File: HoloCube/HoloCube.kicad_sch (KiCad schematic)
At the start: 26 parts, among them J1 ESPProgUART_RX, J2 Conn_01x08_MountingPin, J3 USB_C_Receptacle_USB2.0, U1 ESP32-PICO-D4, U2 LIS2DE12, U3 BH1750FVI-TR, U4 XC6209

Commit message: Place Parts
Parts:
- removed C?: (no value), symbol Device:C
- removed D2, D4: LED, LED_SMD:LED_0603_1608Metric, symbol Device:LED
- removed R?: (no value), symbol Device:R
- removed U2: LIS2DE12, Package_LGA:LGA-12_2x2mm_P0.5mm, symbol Sensor_Motion:LIS2DE12
- removed U3: BH1750FVI-TR, symbol KisonNew:BH1750FVI-TR
- added C4: (no value), symbol Device:C
- added C7, C8: (no value), Capacitor_SMD:C_0603_1608Metric, symbol Device:C
- added C9: TBD, Capacitor_SMD:C_0603_1608Metric, symbol Device:C
- added J4: (no value), symbol Connector:Micro_SD_Card
- added J5: (no value), symbol KisonNew:ESPProgJTAG_RX
- added JP1, JP2: (no value), symbol Jumper:Jumper_2_Bridged
- added R10, R11, R12, R13, R3, R9: (no value), symbol Device:R
- added R14, R15, R16, R17: 10k, Resistor_SMD:R_0603_1608Metric, symbol Device:R
- added U2: (no value), symbol LIS2DH12TR:LIS2DH12TR
- added U3: (no value), symbol BH1750FVI-TR:BH1750FVI-TR
- AE1: value Antenna -> (none); footprint RF_Antenna:Texas_SWRA117D_2.4GHz_Right -> (none)
- C1: value 10uf -> (none)
- C2: value 0.1uf -> (none)
- C3: value 0.1uF -> (none); footprint Capacitor_SMD:C_0603_1608Metric -> (none)
- C5, C6: value 1uf -> (none); footprint Capacitor_SMD:C_0603_1608Metric -> (none)
- D1: value WS2812B -> (none); footprint LED_SMD:LED_WS2812B_PLCC4_5.0x5.0mm_P3.2mm -> (none)
- D3: value D -> (none); footprint KisonNew:C8678 -> (none)
- J1: value ESPProgUART_RX -> (none); footprint KisonNew:IDC_1.27mm_6P -> (none)
- J2: value Conn_01x08_MountingPin -> (none)
- J3: value USB_C_Receptacle_USB2.0 -> (none); footprint Connector_USB:USB_C_Receptacle_HRO_TYPE-C-31-M-12 -> (none)
- R1: value 10k -> (none); footprint Resistor_SMD:R_0603_1608Metric -> (none)
- R2: value 0 -> (none)
- R4: value 0 -> (none); footprint Resistor_SMD:R_0603_1608Metric -> (none)
- R5, R8: value 10k -> (none); footprint Resistor_SMD:R_0603_1608Metric -> (none); LCSC (none) -> C429617
- R6, R7: value 5.1k -> (none); footprint Resistor_SMD:R_0603_1608Metric -> (none)
- U1: value ESP32-PICO-D4 -> (none); footprint Package_DFN_QFN:QFN-48-1EP_7x7mm_P0.5mm_EP5.3x5.3mm -> (none)
- U4: value XC6209 -> (none); footprint Package_TO_SOT_SMD:SOT-23-5 -> (none)
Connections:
- net +3.3VA: now also C1.1, C2.1, R3.2; no longer C1.2, C2.2
- net +3V3: now also J2.7 (Pin_7), R5.1, C4.1, J4.4 (VDD), J5.1 (VDD), JP2.1 (A), R12.2, R14.1, R15.1, R16.1, R17.1, R3.1, R9.1, U2.10 (VDD_IO), U2.2 (CS), U2.9 (VDD), U3.1 (VCC); no longer C1.1, C2.1
- net +5V: now also C5.1, J2.8 (Pin_8), U4.1 (VIN), U4.3 (CE)
- net DC: now also J2.5 (Pin_5), U1.22 (IO2), R10.1
- net GND: now also C1.2, C2.2, J2.6 (Pin_6), C4.2, C7.1, C9.1, J4.6 (VSS), J5.3 (GND), J5.5 (GND), J5.7 (GND), J5.9 (GND), JP1.1 (A), R10.2, R11.2, R13.2, U2.5 (RES), U2.6 (GND), U2.7 (GND), U2.8 (GND), U3.3 (GND)
- net I2C_SCL: now also R5.2, U1.13 (IO33), U2.1 (SCL/SPC), U3.6 (SCL)
- net I2C_SDA: now also R8.2, U1.12 (IO32), U2.4 (SDA/SDI/SDO), U3.4 (SDA)
- net IO18: now also J2.4 (Pin_4), U1.35 (IO18)
- net IO23: now also J2.3 (Pin_3), U1.36 (IO23)
- net IO26: now also U1.15 (IO26), J4.7 (DAT0), R14.2
- net IO27: now also U1.16 (IO27)
- net IO4: now also J2.2 (Pin_2), U1.24 (IO4)
- net IO5: now also J2.1 (Pin_1), U1.34 (IO5)
- net at AE1.1 (A): now also C8.2, C9.2; no longer U1.2 (LNA_IN)
- net IO25: now reaches U1.14 (IO25)
- net IO25: now also J4.3 (CMD), R15.2
- net TMS: now reaches U1.17 (IO14)
- net TMS: now also J5.2 (TMS)
- net TDI: now reaches U1.18 (IO12)
- net TDI: now also J5.8 (TDI)
- net TCLK: now reaches U1.20 (IO13)
- net TCLK: now also J5.4 (TCK)
- net TDO: now reaches U1.21 (IO15)
- net TDO: now also J5.6 (TDO)
- net IO19: now reaches U1.38 (IO19)
- net IO19: now also J4.5 (CLK), R16.2
- net IO22: now reaches U1.39 (IO22)
- net IO21: now reaches U1.42 (IO21)
- net IO21: now also J4.2 (DAT3/CD), R17.2
- removed net EXT_5V: C5.1, R5.1, U4.1 (VIN), U4.3 (CE)
- new net: J4.9 (SHIELD), R11.1
- new net: JP2.2 (B), R13.1, U3.2 (ADDR)
- new net: R9.2, U3.5 (DVI)
- new net: JP1.2 (B), R12.1, U2.3 (SDO/SAO)
- new net: C7.2, C8.1, U1.2 (LNA_IN)
- no-connect marks 2 -> 25
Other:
- note added: "I2C上拉"
- note added: "Just in case if can't enter serial bootloader"
- note added: "LDO"
- note added: "should it have esd?"
- note added: "加速度计"
- note added: "滤波"
- note added: "环境光传感器"
- note removed: "注意检查IO2与IO4的设计要求,确保不影响Boot或直接换Pin"
- note removed: "注意检查与 LIS2DH12TR 的区别，别忘了（"
- moved on the sheet: AE1, C1, C2, C3, C5, C6, D1, D3, J1, J2, J3, R1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

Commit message: Random Version 0.0
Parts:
- removed C4: (no value), symbol Device:C
- removed J5: (no value), symbol KisonNew:ESPProgJTAG_RX
- removed JP2: (no value), symbol Jumper:Jumper_2_Bridged
- removed R10, R13, R3, R9: (no value), symbol Device:R
- removed U3: (no value), symbol BH1750FVI-TR:BH1750FVI-TR
- AE1: value (none) -> Antenna; footprint (none) -> RF_Antenna:Texas_SWRA117D_2.4GHz_Right
- C1: value (none) -> 10uf; footprint (none) -> Capacitor_SMD:C_0603_1608Metric
- C2: value (none) -> 0.1uf; footprint (none) -> Capacitor_SMD:C_0402_1005Metric
- C3: value (none) -> 0.1uF; footprint (none) -> Capacitor_SMD:C_0402_1005Metric
- C5, C6: value (none) -> 1uf; footprint (none) -> Capacitor_SMD:C_0402_1005Metric
- C7: value (none) -> TBD; footprint Capacitor_SMD:C_0603_1608Metric -> Capacitor_SMD:C_0402_1005Metric
- C8: value (none) -> 10pf; footprint Capacitor_SMD:C_0603_1608Metric -> Capacitor_SMD:C_0402_1005Metric
- C9: footprint Capacitor_SMD:C_0603_1608Metric -> Capacitor_SMD:C_0402_1005Metric
- D1: value (none) -> WS2812B; footprint (none) -> LED_SMD:LED_WS2812B_PLCC4_5.0x5.0mm_P3.2mm
- D3: value (none) -> D; footprint (none) -> KisonNew:C8678
- J1: value (none) -> ESPProgUART_RX; footprint (none) -> KisonNew:IDC_1.27mm_6P
- J2: value (none) -> Conn_01x08_MountingPin; footprint (none) -> Connector_FFC-FPC:TE_0-1734839-8_1x08-1MP_P0.5mm_Horizontal
- J3: value (none) -> USB_C_Receptacle_USB2.0; footprint (none) -> Connector_USB:USB_C_Receptacle_HRO_TYPE-C-31-M-12
- J4: value (none) -> Micro_SD_Card; footprint (none) -> KisonNew:C91145
- JP1: value (none) -> Jumper; footprint (none) -> Resistor_SMD:R_0402_1005Metric
- R1: value (none) -> 10k; footprint (none) -> Resistor_SMD:R_0402_1005Metric
- R11, R2, R4: value (none) -> 0; footprint (none) -> Resistor_SMD:R_0402_1005Metric
- R12: value (none) -> 100k; footprint (none) -> Resistor_SMD:R_0402_1005Metric
- R14, R15, R16, R17: footprint Resistor_SMD:R_0603_1608Metric -> Resistor_SMD:R_0402_1005Metric
- R5, R8: value (none) -> 3.3k; footprint (none) -> Resistor_SMD:R_0402_1005Metric
- R6, R7: value (none) -> 5.1k; footprint (none) -> Resistor_SMD:R_0402_1005Metric
- U1: value (none) -> ESP32-PICO-D4; footprint (none) -> Package_DFN_QFN:QFN-48-1EP_7x7mm_P0.5mm_EP5.3x5.3mm
- U2: value (none) -> LIS2DH12TR; footprint (none) -> PQFN50P200X200100-12N
- U4: value (none) -> XC6209; footprint (none) -> Package_TO_SOT_SMD:SOT-23-5
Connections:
- net +3.3VA is gone; now on net +3V3: C1.1, C2.1, U1.1 (VDDA), U1.19 (VDD3P3_RTC), U1.3 (VDDA3P3), U1.37 (VDD3P3_CPU), U1.4 (VDDA3P3), U1.43 (VDDA), U1.46 (VDDA)
- net TDO is gone; now on net IO15: U1.21 (IO15)
- net +3V3: now also R2.1; no longer R2.2
- net DC: now also U1.36 (IO23); no longer U1.22 (IO2)
- net GND: no longer U2.6 (GND), U2.7 (GND)
- net IO19: now also D1.4 (DIN); no longer J4.5 (CLK), R16.2
- net IO22: now also J2.1 (Pin_1)
- net IO25: now also J4.7 (DAT0), R14.2; no longer J4.3 (CMD), R15.2
- net IO26: now also J4.5 (CLK), R16.2; no longer J4.7 (DAT0), R14.2
- net IO27: no longer D1.4 (DIN)
- net IO5: now also J2.3 (Pin_3); no longer J2.1 (Pin_1)
- net at J1.2 (VDD): now also R2.2; no longer R2.1
- net IO21 renamed IO15
- net IO15: no longer U1.42 (IO21)
- removed net IO23: J2.3 (Pin_3), U1.36 (IO23)
- net TCLK renamed IO13
- net IO13: now also J4.3 (CMD), R15.2
- net TDI renamed IO12
- no-connect marks 25 -> 26
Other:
- note removed: "Just in case if can't enter serial bootloader"
- note removed: "环境光传感器"
- note removed: "记得检查各个I2C地址"
- moved on the sheet: J2, R2

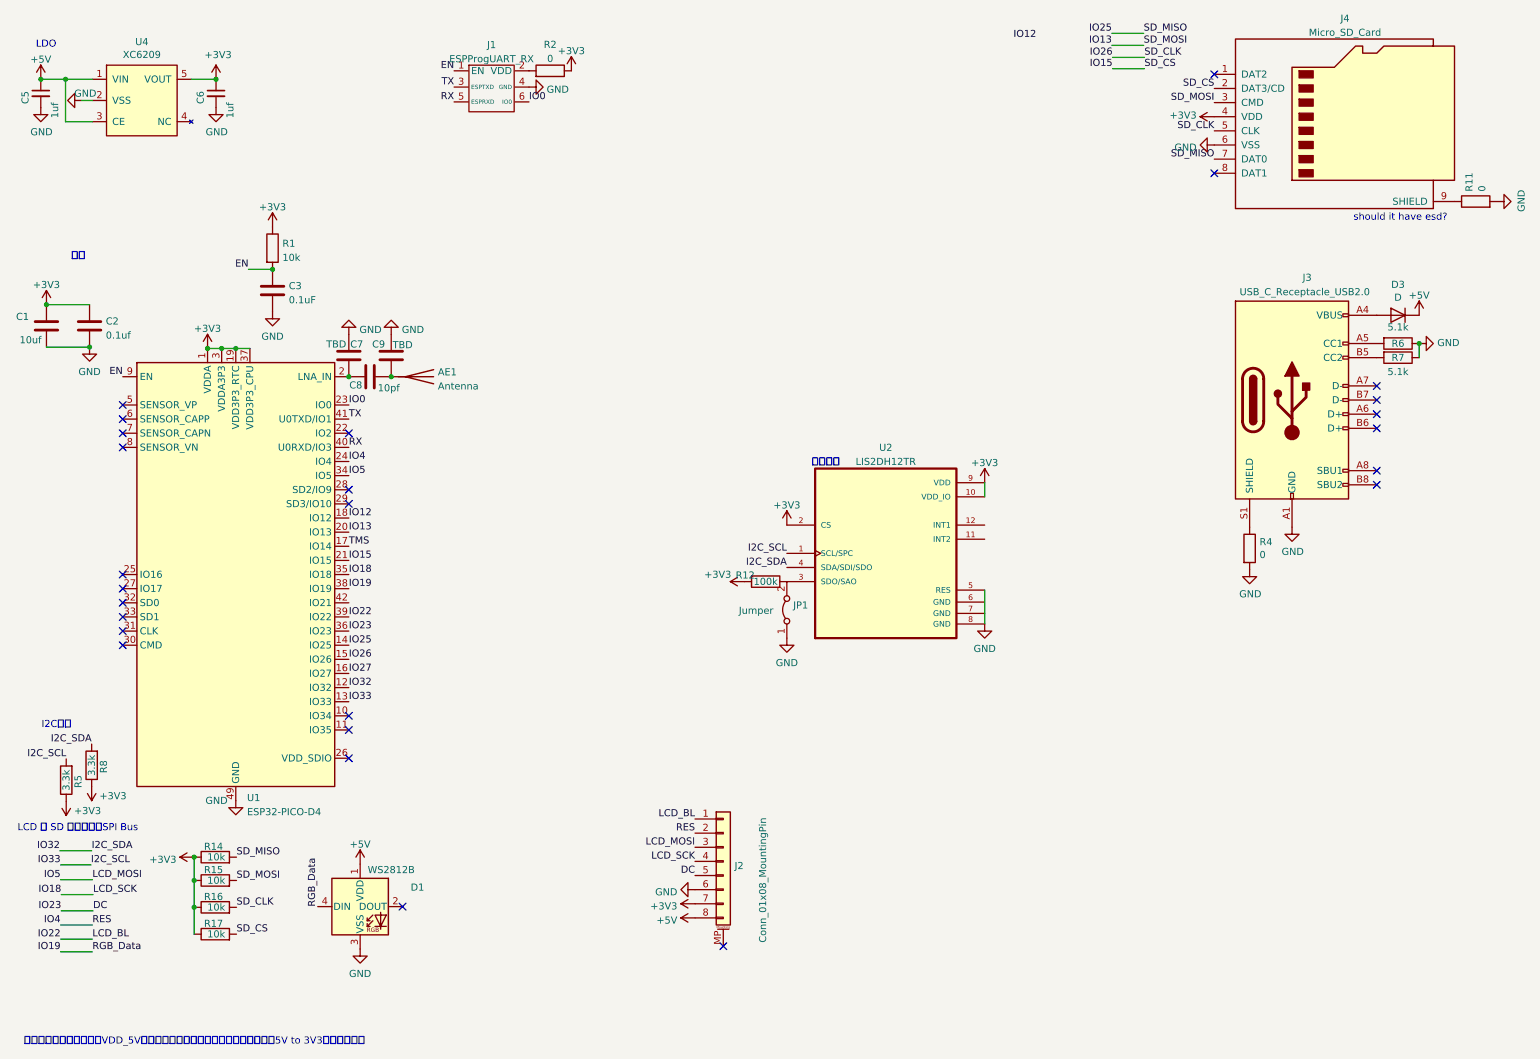
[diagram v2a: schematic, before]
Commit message: Improve According to t123yh
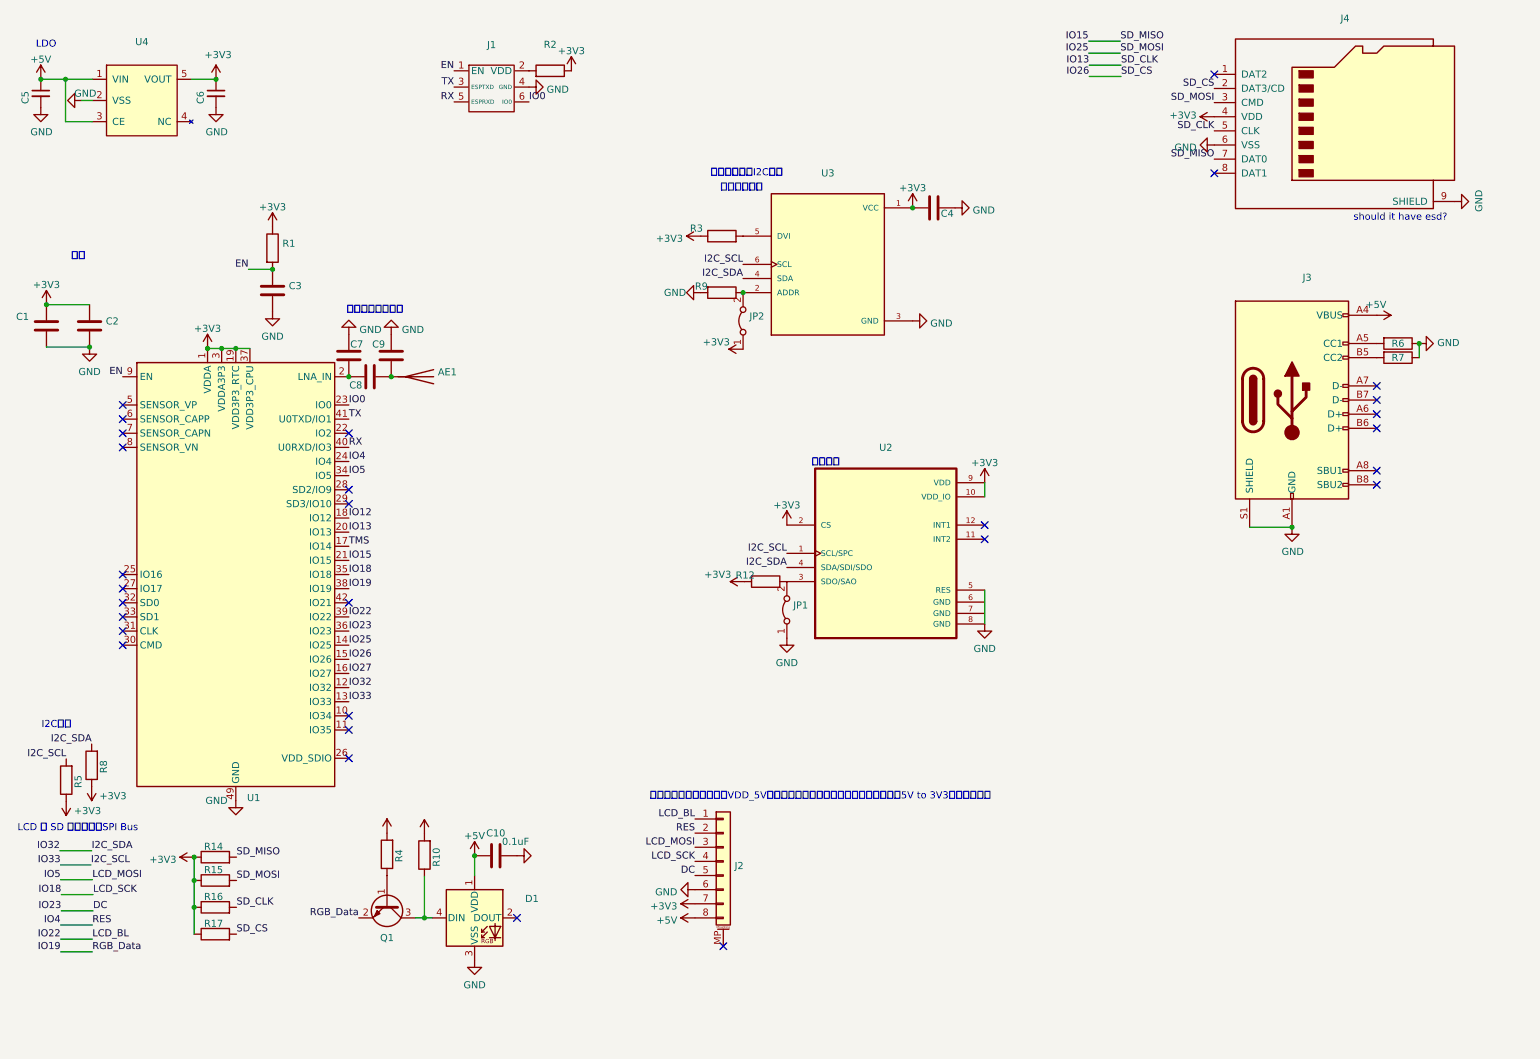
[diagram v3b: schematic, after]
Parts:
- removed D3: D, KisonNew:C8678, symbol Device:D
- removed R11: 0, Resistor_SMD:R_0402_1005Metric, symbol Device:R
- added C10: 0.1uF, Capacitor_SMD:C_0402_1005Metric, symbol Device:C
- added C4: (no value), symbol Device:C
- added JP2: (no value), symbol Jumper:Jumper_2_Bridged
- added Q1: (no value), symbol Transistor_BJT:MMBT3904
- added R10: (no value), Resistor_SMD:R_0402_1005Metric, symbol Device:R
- added R3, R9: (no value), symbol Device:R
- added U3: (no value), symbol BH1750FVI-TR:BH1750FVI-TR
- AE1: value Antenna -> (none); footprint RF_Antenna:Texas_SWRA117D_2.4GHz_Right -> (none)
- C1: value 10uf -> (none); footprint Capacitor_SMD:C_0603_1608Metric -> (none)
- C2: value 0.1uf -> (none); footprint Capacitor_SMD:C_0402_1005Metric -> (none)
- C3: value 0.1uF -> (none); footprint Capacitor_SMD:C_0402_1005Metric -> (none)
- C5, C6: value 1uf -> (none); footprint Capacitor_SMD:C_0402_1005Metric -> (none)
- C7, C9: value TBD -> (none); footprint Capacitor_SMD:C_0402_1005Metric -> (none)
- C8: value 10pf -> (none); footprint Capacitor_SMD:C_0402_1005Metric -> (none)
- D1: value WS2812B -> (none); footprint LED_SMD:LED_WS2812B_PLCC4_5.0x5.0mm_P3.2mm -> (none)
- J1: value ESPProgUART_RX -> (none); footprint KisonNew:IDC_1.27mm_6P -> (none)
- J2: value Conn_01x08_MountingPin -> (none); footprint Connector_FFC-FPC:TE_0-1734839-8_1x08-1MP_P0.5mm_Horizontal -> (none)
- J3: value USB_C_Receptacle_USB2.0 -> (none); footprint Connector_USB:USB_C_Receptacle_HRO_TYPE-C-31-M-12 -> (none)
- J4: value Micro_SD_Card -> (none); footprint KisonNew:C91145 -> (none)
- JP1: value Jumper -> (none); footprint Resistor_SMD:R_0402_1005Metric -> (none)
- R1, R14, R15, R16, R17: value 10k -> (none); footprint Resistor_SMD:R_0402_1005Metric -> (none)
- R12: value 100k -> (none); footprint Resistor_SMD:R_0402_1005Metric -> (none)
- R2: value 0 -> (none); footprint Resistor_SMD:R_0402_1005Metric -> (none)
- R4: value 0 -> (none)
- R5, R8: value 3.3k -> (none); footprint Resistor_SMD:R_0402_1005Metric -> (none)
- R6, R7: value 5.1k -> (none); footprint Resistor_SMD:R_0402_1005Metric -> (none)
- U1: value ESP32-PICO-D4 -> (none); footprint Package_DFN_QFN:QFN-48-1EP_7x7mm_P0.5mm_EP5.3x5.3mm -> (none)
- U2: value LIS2DH12TR -> (none); footprint PQFN50P200X200100-12N -> (none)
- U4: value XC6209 -> (none); footprint Package_TO_SOT_SMD:SOT-23-5 -> (none)
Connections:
- net +3V3: now also R4.2, C4.1, JP2.1 (A), R3.1, U3.1 (VCC)
- net +5V: now also J3.A4 (VBUS), J3.A9 (VBUS), J3.B4 (VBUS), J3.B9 (VBUS), C10.1, R10.2
- net GND: now also J3.S1 (SHIELD), J4.9 (SHIELD), C10.2, C4.2, R9.2, U3.3 (GND); no longer R4.2
- net I2C_SCL: now also U3.6 (SCL)
- net I2C_SDA: now also U3.4 (SDA)
- net IO13: now also J4.5 (CLK), R16.2; no longer J4.3 (CMD), R15.2
- net IO15: now also J4.7 (DAT0), R14.2; no longer J4.2 (DAT3/CD), R17.2
- net IO19: now also Q1.2 (E); no longer D1.4 (DIN)
- net IO25: now also J4.3 (CMD), R15.2; no longer J4.7 (DAT0), R14.2
- net IO26: now also J4.2 (DAT3/CD), R17.2; no longer J4.5 (CLK), R16.2
- net at R4.1: now also Q1.1 (B); no longer J3.S1 (SHIELD)
- new net: R3.2, U3.5 (DVI)
- new net: D1.4 (DIN), Q1.3 (C), R10.1
- new net: JP2.2 (B), R9.1, U3.2 (ADDR)
- no-connect marks 26 -> 29
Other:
- note added: "智慧君的扩展板上，这个VDD_5V其实没用到，可以考虑扩展板上放个额外的5V to 3V3继续降低发热"
- note added: "环境光传感器"
- note added: "留个位置免得麻烦"
- note added: "记得检查各个I2C地址"
- note removed: "智慧君的扩展板上，有个VDD_5V其实没用到，可以考虑扩展板上放个额外的5V to 3V3继续降低发热"
- moved on the sheet: D1

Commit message: Improve again
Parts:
- AE1: value (none) -> Antenna; footprint (none) -> RF_Antenna:Texas_SWRA117D_2.4GHz_Right
- C1: value (none) -> 10uf; footprint (none) -> Capacitor_SMD:C_0603_1608Metric
- C2, C4: value (none) -> 0.1uf; footprint (none) -> Capacitor_SMD:C_0402_1005Metric
- C3: value (none) -> 0.1uF; footprint (none) -> Capacitor_SMD:C_0402_1005Metric
- C5, C6: value (none) -> 1uf; footprint (none) -> Capacitor_SMD:C_0402_1005Metric
- C7, C9: value (none) -> TBD; footprint (none) -> Capacitor_SMD:C_0402_1005Metric
- C8: value (none) -> 10pf; footprint (none) -> Capacitor_SMD:C_0402_1005Metric
- D1: value (none) -> WS2812B; footprint (none) -> LED_SMD:LED_WS2812B_PLCC4_5.0x5.0mm_P3.2mm
- J1: value (none) -> ESPProgUART_RX; footprint (none) -> KisonNew:IDC_1.27mm_6P
- J2: value (none) -> Conn_01x08_MountingPin; footprint (none) -> Connector_FFC-FPC:TE_0-1734839-8_1x08-1MP_P0.5mm_Horizontal
- J3: value (none) -> USB_C_Receptacle_USB2.0; footprint (none) -> Connector_USB:USB_C_Receptacle_HRO_TYPE-C-31-M-12
- J4: value (none) -> Micro_SD_Card; footprint (none) -> KisonNew:C91145
- JP1, JP2: value (none) -> Jumper; footprint (none) -> Resistor_SMD:R_0402_1005Metric
- Q1: value (none) -> MMBT3904; footprint (none) -> Package_TO_SOT_SMD:SOT-23
- R1, R14, R15, R16, R17, R3: value (none) -> 10k; footprint (none) -> Resistor_SMD:R_0402_1005Metric
- R10: value (none) -> 10k
- R12, R9: value (none) -> 100k; footprint (none) -> Resistor_SMD:R_0402_1005Metric
- R2: value (none) -> 0; footprint (none) -> Resistor_SMD:R_0402_1005Metric
- R4: value (none) -> 1.5k
- R5, R8: value (none) -> 3.3k; footprint (none) -> Resistor_SMD:R_0402_1005Metric
- R6, R7: value (none) -> 5.1k; footprint (none) -> Resistor_SMD:R_0402_1005Metric
- U1: value (none) -> ESP32-PICO-D4; footprint (none) -> Package_DFN_QFN:QFN-48-1EP_7x7mm_P0.5mm_EP5.3x5.3mm
- U2: value (none) -> LIS2DH12TR; footprint (none) -> PQFN50P200X200100-12N
- U3: value (none) -> BH1750FVI-TR; footprint (none) -> XDCR_BH1750FVI-TR
- U4: value (none) -> XC6209; footprint (none) -> Package_TO_SOT_SMD:SOT-23-5
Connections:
- net GND: now also J2.MP (MountPin)
- no-connect marks 29 -> 28
